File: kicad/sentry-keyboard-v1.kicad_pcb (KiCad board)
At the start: 2 copper layers, 315 x 121 mm, 269 parts, among them J2 Conn_01x04, J4 AVR-ISP-6, SW1 Reset, SW2 RotaryEncoder_Switch, U1 ATmega32U4-AU, Y1 16Mhz

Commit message: Update footprints and adjust positioning
I printed out the schematic and compare with the physical board and
needed to make some adjustments.
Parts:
- MXenter1: footprint Kaihl hotswap:MX-Hotswap-2.25U -> Kaihl hotswap:MX-Hotswap-2.25U-ReversedStabilizers
- MXspace1: footprint Kaihl hotswap:MX-Hotswap-6.25U -> Kaihl hotswap:MX-Hotswap-6.25U-ReversedStabilizers
- moved SW1 3.89 mm to (166.8, 189.6)
- moved MXpgup1 2.11 mm to (355.5, 170.4)
- moved D103 2.11 mm to (355.6, 175.3)
- moved D133 2.11 mm to (355.8, 156.2)
- moved D134 2.11 mm to (355.7, 137.1)
- moved D135 2.11 mm to (355.3, 118.1)
- moved D43 2.11 mm to (362.7, 155.1)
- moved D53 2.11 mm to (362.7, 136.0)
- moved D61 2.11 mm to (362.7, 174.5)
- moved D72 2.11 mm to (362.6, 117.4)
- moved MXend1 2.11 mm to (355.4, 132.4)
- moved MXhome1 2.11 mm to (355.5, 151.4)
- moved MXpgdn1 2.11 mm to (355.4, 113.4)
- moved R6 0.18 mm to (341.5, 121.9)
- moved R7 0.18 mm to (338.0, 121.9)
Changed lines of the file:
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@@
 	(footprint "Diode_SMD:D_SOD-123"
 		(layer "B.Cu")
-		(at 362.726451 157.191468 180)
+		(at 362.726451 155.083286 180)
 		(descr "SOD-123")
 		(tags "SOD-123")
@@
 	(footprint "Keebio:SK6812-MINI-E"
 		(layer "B.Cu")
-		(at 355.838748 158.332964 180)
+		(at 355.838748 156.224782 180)
 		(property "Reference" "D133"
 			(at 0 -2.1 0)
@@
 	(footprint "Kaihl hotswap:MX-Hotswap-1U"
 		(layer "B.Cu")
-		(at 355.429206 134.47342 180)
+		(at 355.429206 132.365238 180)
 		(property "Reference" "MXend1"
 			(at 0 -3.175 0)
@@
 	(footprint "Diode_SMD:D_SOD-123"
 		(layer "B.Cu")
-		(at 362.658564 176.608182 180)
+		(at 362.658564 174.5 180)
 		(descr "SOD-123")
 		(tags "SOD-123")
@@
 	(footprint "Keebio:SK6812-MINI-E"
 		(layer "B.Cu")
-		(at 355.675 139.25 180)
+		(at 355.675 137.141818 180)
 		(property "Reference" "D134"
 			(at 0 -2.1 0)
@@
 	(footprint "Keebio:SK6812-MINI-E"
 		(layer "B.Cu")
-		(at 355.325 120.25 180)
+		(at 355.325 118.141818 180)
 		(property "Reference" "D135"
 			(at 0 -2.1 0)
@@
 		)
 	)
-	(footprint "Kaihl hotswap:MX-Hotswap-6.25U"
+	(footprint "Kaihl hotswap:MX-Hotswap-6.25U-ReversedStabilizers"
 		(layer "B.Cu")
 		(at 183.22952 189.486557 180)
@@
 		)
 		(pad "" np_thru_hole circle
-			(at -50 -8.255 180)
-			(size 3.9878 3.9878)
-			(drill 3.9878)
+			(at -50 -6.985 180)
+			(size 3.048 3.048)
+			(drill 3.048)
 			(layers "*.Cu" "*.Mask")
 		)
 		(pad "" np_thru_hole circle
-			(at -50 6.985 180)
-			(size 3.048 3.048)
-			(drill 3.048)
+			(at -50 8.255 180)
+			(size 3.9878 3.9878)
+			(drill 3.9878)
 			(layers "*.Cu" "*.Mask")
 		)
@@
 		)
 		(pad "" np_thru_hole circle
-			(at 50 -8.255 180)
-			(size 3.9878 3.9878)
-			(drill 3.9878)
+			(at 50 -6.985 180)
+			(size 3.048 3.048)
+			(drill 3.048)
 			(layers "*.Cu" "*.Mask")
 		)
 		(pad "" np_thru_hole circle
-			(at 50 6.985 180)
-			(size 3.048 3.048)
-			(drill 3.048)
+			(at 50 8.255 180)
+			(size 3.9878 3.9878)
+			(drill 3.9878)
 			(layers "*.Cu" "*.Mask")
 		)
@@
 	(footprint "Keebio:SW_SPST_TL3342"
 		(layer "B.Cu")
-		(at 169.65 186.9 180)
+		(at 166.85 189.6 180)
 		(descr "Low-profile SMD Tactile Switch, https://www.e-switch.com/system/asset/product_line/data_sheet/165/TL3342.pdf")
 		(tags "SPST Tactile Switch")
@@
 	(footprint "Kaihl hotswap:MX-Hotswap-1U"
 		(layer "B.Cu")
-		(at 355.5 153.5 180)
+		(at 355.5 151.391818 180)
 		(property "Reference" "MXhome1"
 			(at 0 -3.175 0)
@@
 	(footprint "Keebio:SK6812-MINI-E"
 		(layer "B.Cu")
-		(at 355.640299 177.455276 180)
+		(at 355.640299 175.347094 180)
 		(property "Reference" "D103"
 			(at 0 -2.1 0)
@@
 	(footprint "Diode_SMD:D_SOD-123"
 		(layer "B.Cu")
-		(at 362.655657 138.154532 180)
+		(at 362.655657 136.04635 180)
 		(descr "SOD-123")
 		(tags "SOD-123")
@@
 	(footprint "Diode_SMD:D_SOD-123"
 		(layer "B.Cu")
-		(at 362.579206 119.51342 180)
+		(at 362.579206 117.405238 180)
 		(descr "SOD-123")
 		(tags "SOD-123")
@@
 	(footprint "Kaihl hotswap:MX-Hotswap-1U"
 		(layer "B.Cu")
-		(at 355.429206 115.51342 180)
+		(at 355.429206 113.405238 180)
 		(property "Reference" "MXpgdn1"
 			(at 0 -3.175 0)
@@
 	(footprint "Kaihl hotswap:MX-Hotswap-1U"
 		(layer "B.Cu")
-		(at 355.504975 172.553984 180)
+		(at 355.504975 170.445802 180)
 		(property "Reference" "MXpgup1"
 			(at 0 -3.175 0)
@@
 	(footprint "Resistor_SMD:R_0805_2012Metric"
 		(layer "B.Cu")
-		(at 338 122.0875 90)
+		(at 338 121.9125 90)
 		(descr "Resistor SMD 0805 (2012 Metric), square (rectangular) end terminal, IPC-7351 nominal, (Body size source: IPC-SM-782 page 72, https://www.pcb-3d.com/wordpress/wp-content/uploads/ipc-sm-782a_amendment_1_and_2.pdf), generated with kicad-footprint-generator")
 		(tags "resistor")
@@
 		)
 	)
-	(footprint "Kaihl hotswap:MX-Hotswap-2.25U"
+	(footprint "Kaihl hotswap:MX-Hotswap-2.25U-ReversedStabilizers"
 		(layer "B.Cu")
 		(at 316.569852 151.375628 180)
@@
 		)
 		(pad "" np_thru_hole circle
-			(at -11.938 -8.255 180)
-			(size 3.9878 3.9878)
-			(drill 3.9878)
+			(at -11.938 -6.985 180)
+			(size 3.048 3.048)
+			(drill 3.048)
 			(layers "*.Cu" "*.Mask")
 		)
 		(pad "" np_thru_hole circle
-			(at -11.938 6.985 180)
-			(size 3.048 3.048)
-			(drill 3.048)
+			(at -11.938 8.255 180)
+			(size 3.9878 3.9878)
+			(drill 3.9878)
 			(layers "*.Cu" "*.Mask")
 		)
@@
 		)
 		(pad "" np_thru_hole circle
-			(at 11.938 -8.255 180)
-			(size 3.9878 3.9878)
-			(drill 3.9878)
+			(at 11.938 -6.985 180)
+			(size 3.048 3.048)
+			(drill 3.048)
 			(layers "*.Cu" "*.Mask")
 		)
 		(pad "" np_thru_hole circle
-			(at 11.938 6.985 180)
-			(size 3.048 3.048)
-			(drill 3.048)
+			(at 11.938 8.255 180)
+			(size 3.9878 3.9878)
+			(drill 3.9878)
 			(layers "*.Cu" "*.Mask")
 		)
@@
 	(footprint "Resistor_SMD:R_0805_2012Metric"
 		(layer "B.Cu")
-		(at 341.5 122.0875 -90)
+		(at 341.5 121.9125 -90)
 		(descr "Resistor SMD 0805 (2012 Metric), square (rectangular) end terminal, IPC-7351 nominal, (Body size source: IPC-SM-782 page 72, https://www.pcb-3d.com/wordpress/wp-content/uploads/ipc-sm-782a_amendment_1_and_2.pdf), generated with kicad-footprint-generator")
 		(tags "resistor")
@@
 		(layer "F.Cu")
 		(pts
+			(xy 370 202.5) (xy 357 172.5)
+		)
+		(height 0)
+		(orientation 1)
+		(format
+			(prefix "")
+			(suffix "")
+			(units 2)
+			(units_format 0)
+			(precision 4)
+			(suppress_zeroes yes)
+		)
+		(style
+			(thickness 0.2)
+			(arrow_length 1.27)
+			(text_position_mode 0)
+			(arrow_direction outward)
+			(extension_height 0.58642)
+			(extension_offset 0.5)
+			(keep_text_aligned yes)
+		)
+		(gr_text "30"
+			(at 368.2 187.5 90)
+			(layer "F.Cu")
+			(effects
+				(font
+					(size 1.5 1.5)
+					(thickness 0.3)
+				)
+			)
+		)
+	)
+	(dimension
+		(type orthogonal)
+		(layer "F.Cu")
+		(pts
 			(xy 51.5 190) (xy 58.5 190)
 		)
@@
 			(layer "F.Cu")
 			(effects
+				(font
+					(size 1.5 1.5)
+					(thickness 0.3)
+				)
+			)
+		)
+	)
+	(dimension
+		(type orthogonal)
+		(layer "F.Cu")
+		(pts
+			(xy 355.429206 115.5) (xy 365 202.5)
+		)
+		(height 16.070794)
+		(orientation 1)
+		(format
+			(prefix "")
+			(suffix "")
+			(units 2)
+			(units_format 0)
+			(precision 4)
+			(suppress_zeroes yes)
+		)
+		(style
+			(thickness 0.2)
+			(arrow_length 1.27)
+			(text_position_mode 0)
+			(arrow_direction outward)
+			(extension_height 0.58642)
+			(extension_offset 0.5)
+			(keep_text_aligned yes)
+		)
+		(gr_text "87"
+			(at 369.7 159 90)
+			(layer "F.Cu")
+			(effects

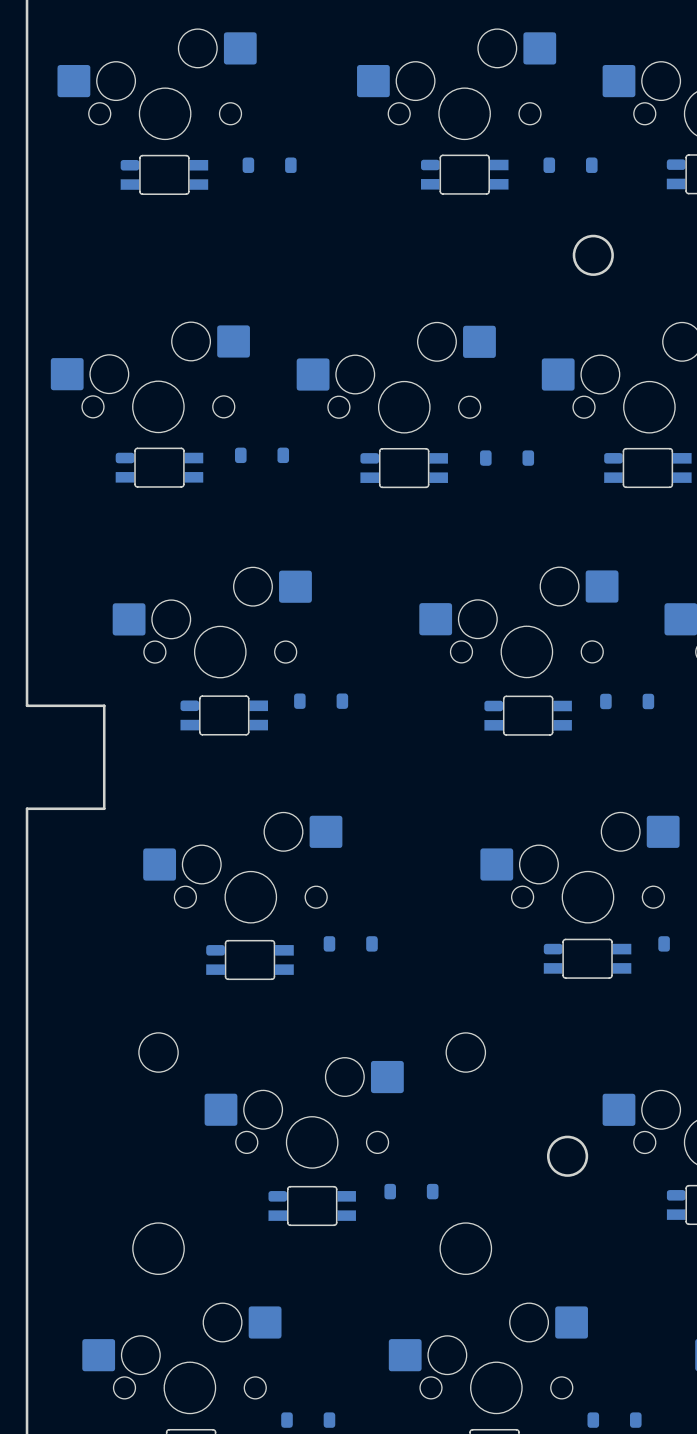
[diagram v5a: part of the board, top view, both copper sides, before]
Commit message: Move measures to user comments and start traces
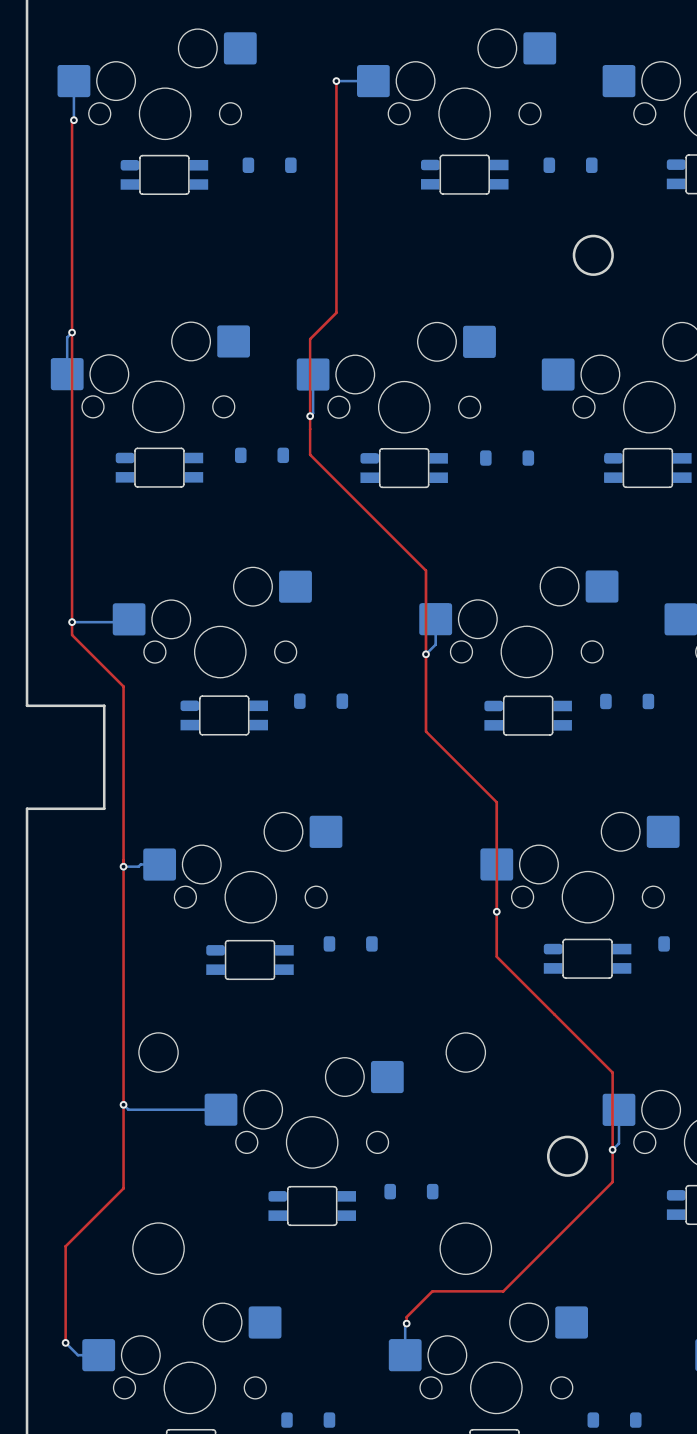
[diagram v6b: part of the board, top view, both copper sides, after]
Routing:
- net Col1: track 0.00 -> 135.7 mm, vias 0 -> 6
- net Col0: track 0.00 -> 123.6 mm, vias 0 -> 6

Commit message: Fix a big schematic mistake
I had two col5 nets! I only noticed this as I started routing the
columns. I also fixed the numbering of all the switches.
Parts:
- F10: value K0_4 -> K0_10
- F11: value K0_5 -> K0_11
- F12: value K0_4 -> K0_12
- F13: value K0_5 -> K0_13
- F6: value K0_0 -> K0_6
- F7: value K0_1 -> K0_7
- F8: value K0_2 -> K0_8
- F9: value K0_3 -> K0_9
- MX'1: value K0_5 -> K3_11
- MX+1: value K0_4 -> K1_12
- MX,1: value K0_2 -> K4_8
- MX-1: value K0_5 -> K1_11
- MX.1: value K0_3 -> K4_9
- MX/1: value K0_4 -> K4_10
- MX0: value K0_4 -> K1_10
- MX6: value K0_0 -> K1_6
- MX7: value K0_1 -> K1_7
- MX8: value K0_2 -> K1_8
- MX9: value K0_3 -> K1_9
- MX;1: value K0_4 -> K3_10
- MX[1: value K0_5 -> K2_11
- MX\1: value K0_5 -> K2_13
- MX]1: value K0_4 -> K2_12
- MXalt1: value K3_2 -> K5_2
- MXb1: value K3_5 -> K4_5
- MXbksp1: value K0_5 -> K1_13
- MXc1: value K3_3 -> K4_3
- MXctrl1: value K3_0 -> K5_0
- MXdown1: value K0_2 -> K5_8
- MXend1: value K0_5 -> K5_11
- MXenter1: value K0_4 -> K3_12
- MXfn1: value K3_5 -> K5_5
- MXh1: value K0_0 -> K3_6
- MXhome1: value K0_5 -> K5_10
- MXi1: value K0_2 -> K2_8
- MXj1: value K0_1 -> K3_7
- MXk1: value K0_2 -> K3_8
- MXl1: value K0_3 -> K3_9
- MXleft1: value K0_1 -> K5_7
- MXlshift1: value K3_0 -> K4_0
- MXm1: value K0_1 -> K4_7
- MXn1: value K0_0 -> K4_6
- MXo1: value K0_3 -> K2_9
- MXp1: value K0_4 -> K2_10
- MXpgdn1: value K0_5 -> K5_12
- MXpgup1: value K0_5 -> K4_13
- MXralt1: value K3_4 -> K5_4
- MXrctrl1: value K0_0 -> K5_6
- MXright1: value K0_3 -> K5_9
- MXrshift1: value K0_5 -> K4_11
- MXspace1: value K3_3 -> K5_3
- MXsuper1: value K3_1 -> K5_1
- MXu1: value K0_1 -> K2_7
- MXup1: value K0_4 -> K4_12
- MXv1: value K3_4 -> K4_4
- MXx1: value K3_2 -> K4_2
- MXy1: value K0_0 -> K2_6
- MXz1: value K3_1 -> K4_1
- moved D61 56.9 mm to (362.7, 117.6)
- moved MXpgup1 56.9 mm to (355.6, 113.5)
- moved D55 38.1 mm to (217.2, 155.2)
- moved MXj1 38.1 mm to (209.4, 151.4)
- moved D24 38.1 mm to (179.0, 155.2)
- moved MXg1 38.1 mm to (171.3, 151.4)
- moved D43 19.2 mm to (362.9, 174.3)
- moved D53 19.2 mm to (362.8, 155.2)
- moved D72 19.2 mm to (362.7, 136.6)
- moved MXhome1 19.2 mm to (355.7, 170.6)
- moved MXpgdn1 19.2 mm to (355.6, 132.6)
- moved MXend1 19.2 mm to (355.6, 151.6)
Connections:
- F10 pad 1: Col9 -> Col10
- F11 pad 1: Col10 -> Col11
- F12 pad 1: Col11 -> Col12
- F13 pad 1: Col12 -> Col13
- F6 pad 1: Col5 -> Col6
- F7 pad 1: Col6 -> Col7
- F8 pad 1: Col7 -> Col8
- F9 pad 1: Col8 -> Col9
- MX'1 pad 1: Col10 -> Col11
- MX+1 pad 1: Col11 -> Col12
- MX,1 pad 1: Col7 -> Col8
- MX-1 pad 1: Col10 -> Col11
- MX.1 pad 1: Col8 -> Col9
- MX/1 pad 1: Col9 -> Col10
- MX0 pad 1: Col9 -> Col10
- MX6 pad 1: Col5 -> Col6
- MX7 pad 1: Col6 -> Col7
- MX8 pad 1: Col7 -> Col8
- MX9 pad 1: Col8 -> Col9
- MX;1 pad 1: Col9 -> Col10
- MX[1 pad 1: Col10 -> Col11
- MX\1 pad 1: Col12 -> Col13
- MX]1 pad 1: Col11 -> Col12
- MXbksp1 pad 1: Col12 -> Col13
- MXdown1 pad 1: Col7 -> Col8
- MXend1 pad 1: Col10 -> Col11
- MXenter1 pad 1: Col11 -> Col12
- MXh1 pad 1: Col5 -> Col6
- MXhome1 pad 1: Col9 -> Col10
- MXi1 pad 1: Col7 -> Col8
- MXj1 pad 1: Col6 -> Col7
- MXk1 pad 1: Col7 -> Col8
- MXl1 pad 1: Col8 -> Col9
- MXleft1 pad 1: Col6 -> Col7
- MXm1 pad 1: Col6 -> Col7
- MXn1 pad 1: Col5 -> Col6
- MXo1 pad 1: Col8 -> Col9
- MXp1 pad 1: Col9 -> Col10
- MXpgdn1 pad 1: Col11 -> Col12
- MXpgup1 pad 1: Col12 -> Col13
- MXrctrl1 pad 1: Col5 -> Col6
- MXright1 pad 1: Col8 -> Col9
- MXrshift1 pad 1: Col10 -> Col11
- MXu1 pad 1: Col6 -> Col7
- MXup1 pad 1: Col11 -> Col12
- MXy1 pad 1: Col5 -> Col6
- U1 pad 40: unconnected-(U1-PF1-Pad40) -> Col13
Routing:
- net Col4: track 0.00 -> 166.9 mm, vias 0 -> 2
- net Col3: track 0.00 -> 159.9 mm, vias 0 -> 6
- net Col2: track 0.00 -> 134.9 mm, vias 0 -> 6
- net Col5: track 0.00 -> 3.08 mm, vias 0 -> 1

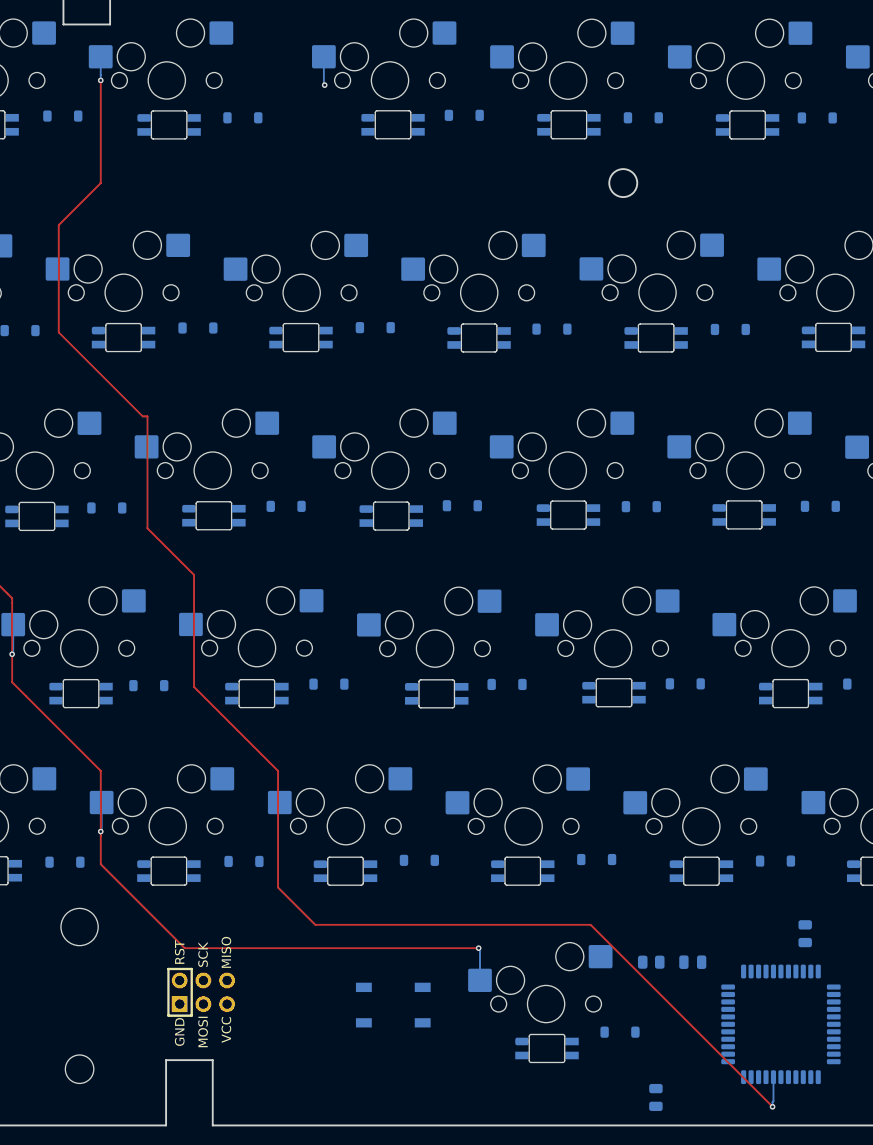
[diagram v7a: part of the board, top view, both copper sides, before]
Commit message: Route more columns
The cpu area needs to be reworked once all the columns are roughed in.
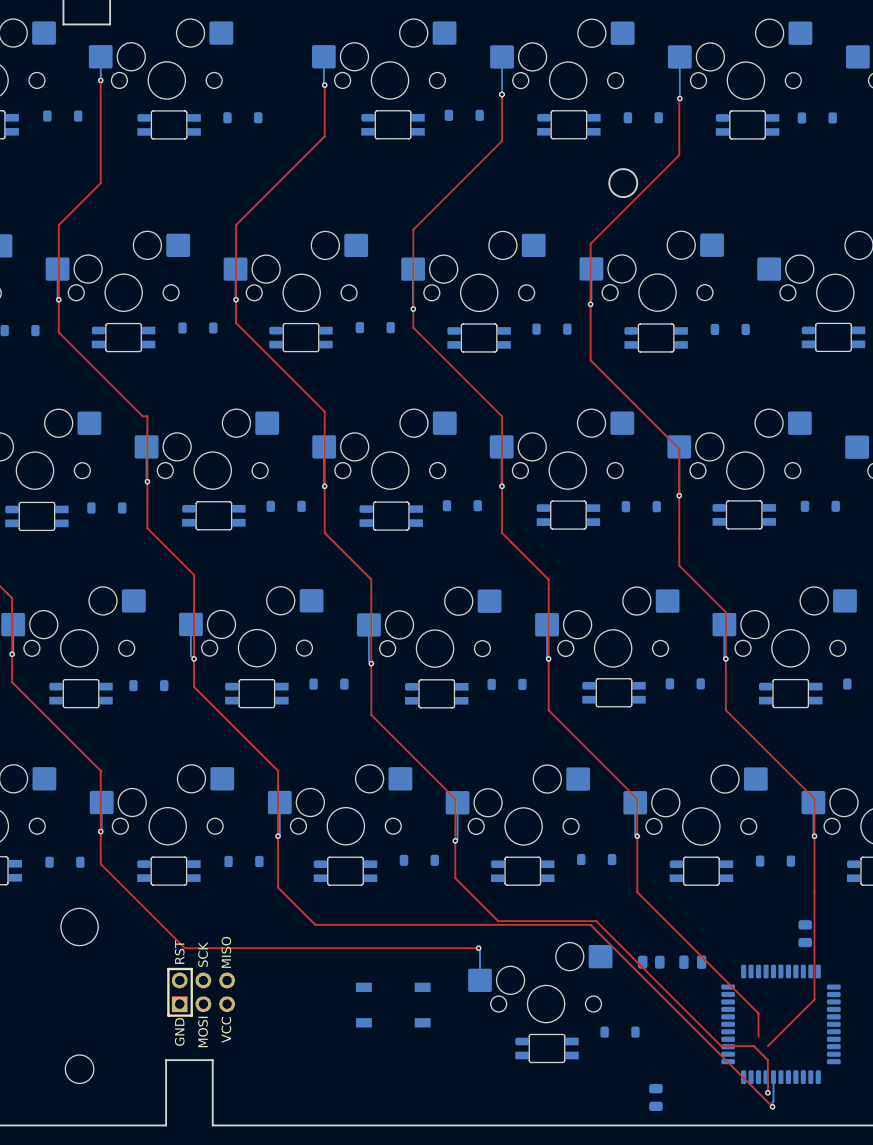
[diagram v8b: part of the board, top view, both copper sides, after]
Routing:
- net Col5: track 3.08 -> 164.6 mm, vias 1 -> 6
- net Col6: track 0.00 -> 140.2 mm, vias 0 -> 6
- net Col7: track 0.00 -> 138.5 mm, vias 0 -> 5
- net Col4: track 166.9 -> 181.5 mm, vias 2 -> 6
